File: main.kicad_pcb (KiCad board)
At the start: 2 copper layers, 31.3 x 52.8 mm, 21 parts

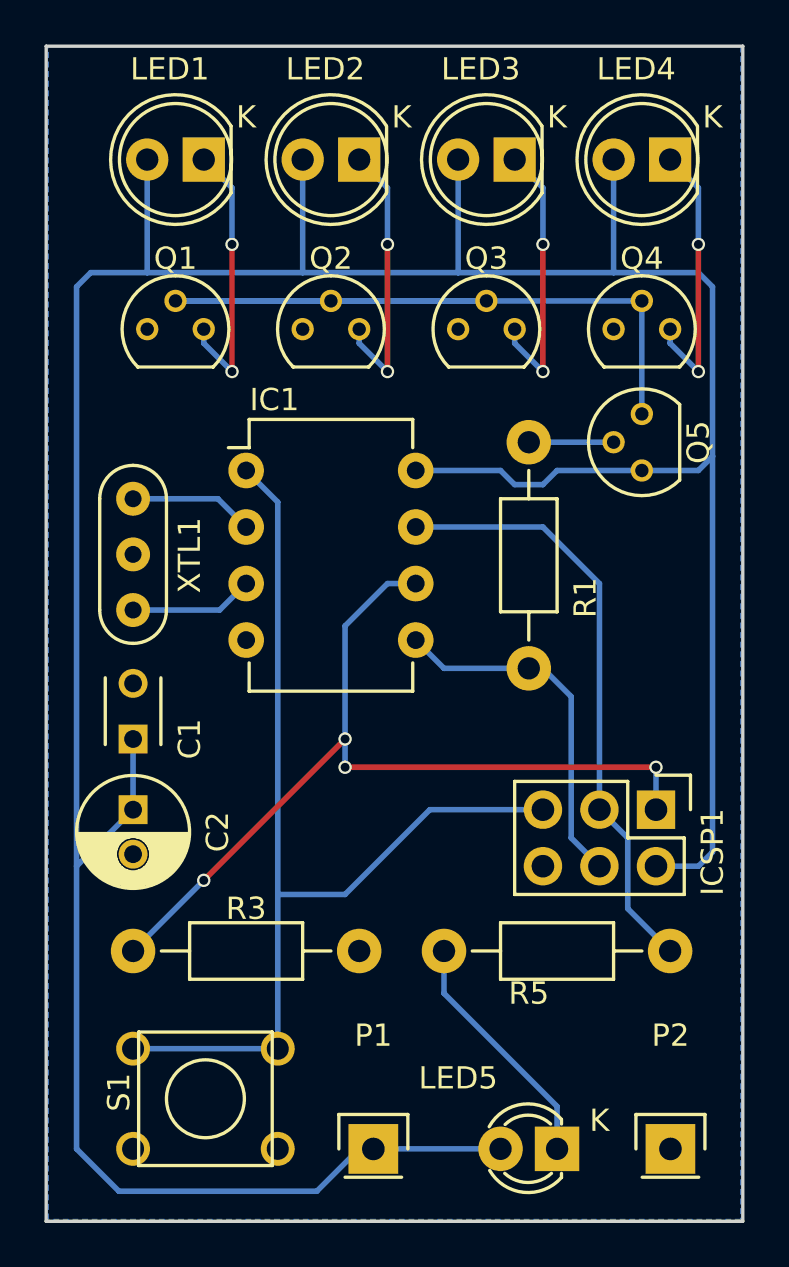
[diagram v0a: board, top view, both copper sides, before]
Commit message: new vias
bigger and better for cnc
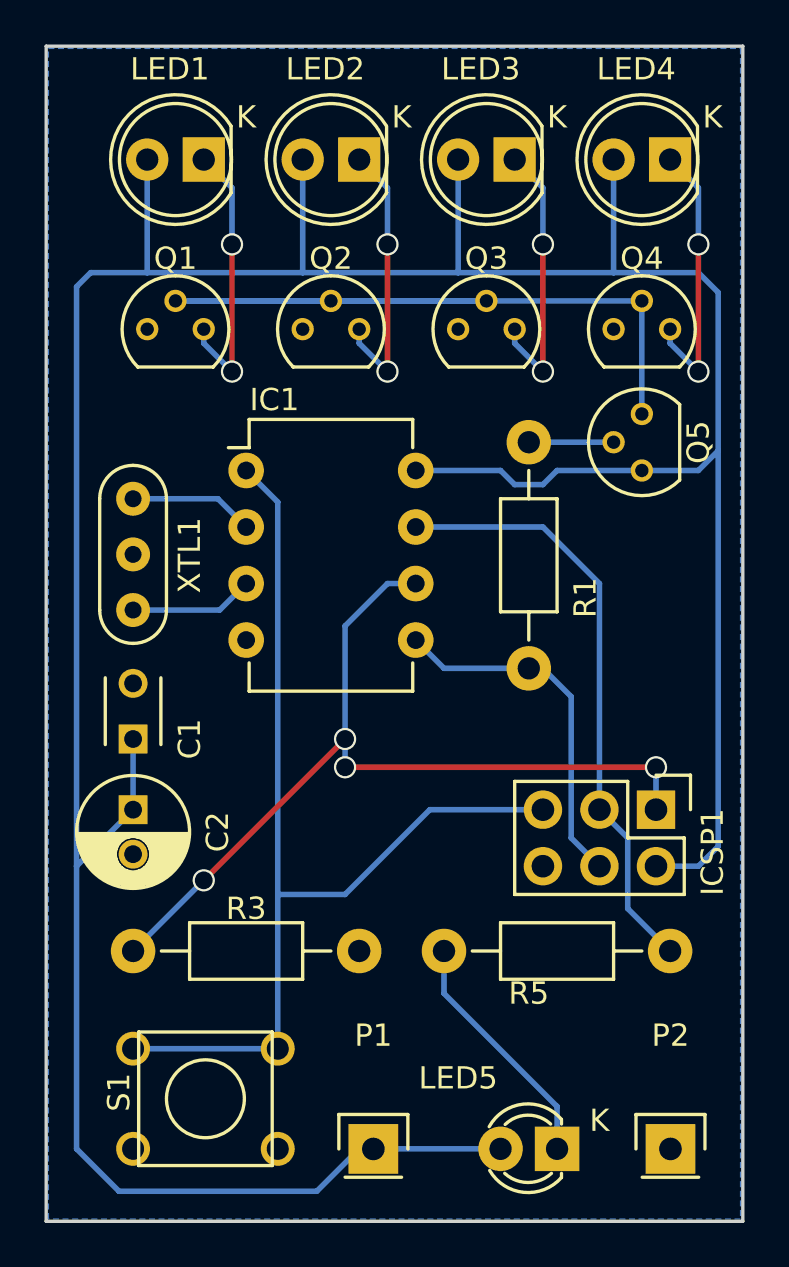
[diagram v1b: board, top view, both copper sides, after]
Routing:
- net VCC: track 158.5 -> 159.1 mm
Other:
- net class Default: via_dia 0.8 -> 1; via_drill 0.7 -> 0.8
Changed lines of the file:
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@@
     (links 43)
     (no_connects 0)
-    (area 148.95 69.106 181.875 122.62)
+    (area 150.324999 69.124999 181.775001 122.075001)
     (thickness 1.6)
     (drawings 5)
@@
     (segment_width 0.2)
     (edge_width 0.15)
-    (via_size 0.8)
-    (via_drill 0.7)
+    (via_size 1)
+    (via_drill 0.8)
     (via_min_size 0.4)
     (via_min_drill 0.3)
@@
     (clearance 0.2)
     (trace_width 0.25)
-    (via_dia 0.8)
-    (via_drill 0.7)
+    (via_dia 1)
+    (via_drill 0.8)
     (uvia_dia 0.3)
     (uvia_drill 0.1)
@@
   )
   (gr_text ".pls GS" (at 177.7 96.2 90) (layer Dwgs.User)
-    (effects (font (size 1.5 1.5) (thickness 0.3)))
+    (effects (font (size 1.5 1.5) (thickness 0.3)) (justify mirror))
   )
   (gr_line (start 150.4 69.2) (end 181.7 69.2) (angle 90) (layer Edge.Cuts) (width 0.15))
@@
   (gr_line (start 150.4 122) (end 181.7 122) (angle 90) (layer Edge.Cuts) (width 0.15))
   (segment (start 152.4 79.375) (end 151.765 80.01) (width 0.25) (layer B.Cu) (net 1))
-  (segment (start 180.34 87.63) (end 180.34 105.41) (width 0.25) (layer B.Cu) (net 1))
+  (segment (start 180.594 87.376) (end 180.594 105.156) (width 0.25) (layer B.Cu) (net 1))
   (segment (start 179.705 106.045) (end 177.8 106.045) (width 0.25) (layer B.Cu) (net 1))
-  (segment (start 180.34 105.41) (end 179.705 106.045) (width 0.25) (layer B.Cu) (net 1))
+  (segment (start 180.594 105.156) (end 179.705 106.045) (width 0.25) (layer B.Cu) (net 1))
   (segment (start 170.815 118.745) (end 170.815 119.38) (width 0.25) (layer B.Cu) (net 1))
   (segment (start 177.165 88.265) (end 173.355 88.265) (width 0.25) (layer B.Cu) (net 1))
@@
   (segment (start 175.895 79.375) (end 179.705 79.375) (width 0.25) (layer B.Cu) (net 1))
   (segment (start 179.705 88.265) (end 177.165 88.265) (width 0.25) (layer B.Cu) (net 1))
-  (segment (start 180.34 87.63) (end 179.705 88.265) (width 0.25) (layer B.Cu) (net 1))
-  (segment (start 180.34 80.01) (end 180.34 87.63) (width 0.25) (layer B.Cu) (net 1))
-  (segment (start 179.705 79.375) (end 180.34 80.01) (width 0.25) (layer B.Cu) (net 1))
+  (segment (start 180.594 87.376) (end 179.705 88.265) (width 0.25) (layer B.Cu) (net 1))
+  (segment (start 180.594 80.264) (end 180.594 87.376) (width 0.25) (layer B.Cu) (net 1))
+  (segment (start 179.705 79.375) (end 180.594 80.264) (width 0.25) (layer B.Cu) (net 1))
   (segment (start 154.94 79.375) (end 154.94 74.295) (width 0.25) (layer B.Cu) (net 1))
   (segment (start 161.925 79.375) (end 161.925 74.295) (width 0.25) (layer B.Cu) (net 1))
@@
   (segment (start 163.83 100.33) (end 163.83 101.6) (width 0.25) (layer B.Cu) (net 7))
   (segment (start 177.8 101.6) (end 177.8 103.505) (width 0.25) (layer B.Cu) (net 7))
-  (via (at 177.8 101.6) (size 0.6) (drill 0.4) (layers F.Cu B.Cu) (net 7))
+  (via (at 177.8 101.6) (size 1) (drill 0.8) (layers F.Cu B.Cu) (net 7))
   (segment (start 163.83 101.6) (end 177.8 101.6) (width 0.25) (layer F.Cu) (net 7))
-  (via (at 163.83 101.6) (size 0.6) (drill 0.4) (layers F.Cu B.Cu) (net 7))
+  (via (at 163.83 101.6) (size 1) (drill 0.8) (layers F.Cu B.Cu) (net 7))
   (segment (start 154.305 109.855) (end 157.48 106.68) (width 0.25) (layer B.Cu) (net 7))
   (segment (start 165.735 93.345) (end 167.005 93.345) (width 0.25) (layer B.Cu) (net 7))
   (segment (start 163.83 95.25) (end 165.735 93.345) (width 0.25) (layer B.Cu) (net 7))
   (segment (start 163.83 100.33) (end 163.83 95.25) (width 0.25) (layer B.Cu) (net 7))
-  (via (at 163.83 100.33) (size 0.6) (drill 0.4) (layers F.Cu B.Cu) (net 7))
+  (via (at 163.83 100.33) (size 1) (drill 0.8) (layers F.Cu B.Cu) (net 7))
   (segment (start 157.48 106.68) (end 163.83 100.33) (width 0.25) (layer F.Cu) (net 7))
-  (via (at 157.48 106.68) (size 0.6) (drill 0.4) (layers F.Cu B.Cu) (net 7))
+  (via (at 157.48 106.68) (size 1) (drill 0.8) (layers F.Cu B.Cu) (net 7))
   (segment (start 178.435 109.855) (end 176.53 107.95) (width 0.25) (layer B.Cu) (net 8))
   (segment (start 176.53 104.775) (end 175.26 103.505) (width 0.25) (layer B.Cu) (net 8))
@@
   (segment (start 158.75 75.565) (end 157.48 74.295) (width 0.25) (layer B.Cu) (net 9))
   (segment (start 158.75 78.105) (end 158.75 75.565) (width 0.25) (layer B.Cu) (net 9))
-  (via (at 158.75 78.105) (size 0.6) (drill 0.4) (layers F.Cu B.Cu) (net 9))
+  (via (at 158.75 78.105) (size 1) (drill 0.8) (layers F.Cu B.Cu) (net 9))
   (segment (start 158.75 83.82) (end 158.75 78.105) (width 0.25) (layer F.Cu) (net 9))
-  (via (at 158.75 83.82) (size 0.6) (drill 0.4) (layers F.Cu B.Cu) (net 9))
+  (via (at 158.75 83.82) (size 1) (drill 0.8) (layers F.Cu B.Cu) (net 9))
   (segment (start 157.48 82.55) (end 158.75 83.82) (width 0.25) (layer B.Cu) (net 9))
   (segment (start 164.465 81.915) (end 164.465 82.55) (width 0.25) (layer B.Cu) (net 10))
   (segment (start 165.735 75.565) (end 164.465 74.295) (width 0.25) (layer B.Cu) (net 10))
   (segment (start 165.735 78.105) (end 165.735 75.565) (width 0.25) (layer B.Cu) (net 10))
-  (via (at 165.735 78.105) (size 0.6) (drill 0.4) (layers F.Cu B.Cu) (net 10))
+  (via (at 165.735 78.105) (size 1) (drill 0.8) (layers F.Cu B.Cu) (net 10))
   (segment (start 165.735 83.82) (end 165.735 78.105) (width 0.25) (layer F.Cu) (net 10))
-  (via (at 165.735 83.82) (size 0.6) (drill 0.4) (layers F.Cu B.Cu) (net 10))
+  (via (at 165.735 83.82) (size 1) (drill 0.8) (layers F.Cu B.Cu) (net 10))
   (segment (start 164.465 82.55) (end 165.735 83.82) (width 0.25) (layer B.Cu) (net 10))
   (segment (start 171.45 81.915) (end 171.45 82.55) (width 0.25) (layer B.Cu) (net 11))
   (segment (start 172.72 75.565) (end 171.45 74.295) (width 0.25) (layer B.Cu) (net 11))
   (segment (start 172.72 78.105) (end 172.72 75.565) (width 0.25) (layer B.Cu) (net 11))
-  (via (at 172.72 78.105) (size 0.6) (drill 0.4) (layers F.Cu B.Cu) (net 11))
+  (via (at 172.72 78.105) (size 1) (drill 0.8) (layers F.Cu B.Cu) (net 11))
   (segment (start 172.72 83.82) (end 172.72 78.105) (width 0.25) (layer F.Cu) (net 11))
-  (via (at 172.72 83.82) (size 0.6) (drill 0.4) (layers F.Cu B.Cu) (net 11))
+  (via (at 172.72 83.82) (size 1) (drill 0.8) (layers F.Cu B.Cu) (net 11))
   (segment (start 171.45 82.55) (end 172.72 83.82) (width 0.25) (layer B.Cu) (net 11))
   (segment (start 178.435 81.915) (end 178.435 82.55) (width 0.25) (layer B.Cu) (net 12))
   (segment (start 179.705 75.565) (end 178.435 74.295) (width 0.25) (layer B.Cu) (net 12))
   (segment (start 179.705 78.105) (end 179.705 75.565) (width 0.25) (layer B.Cu) (net 12))
-  (via (at 179.705 78.105) (size 0.6) (drill 0.4) (layers F.Cu B.Cu) (net 12))
+  (via (at 179.705 78.105) (size 1) (drill 0.8) (layers F.Cu B.Cu) (net 12))
   (segment (start 179.705 83.82) (end 179.705 78.105) (width 0.25) (layer F.Cu) (net 12))
-  (via (at 179.705 83.82) (size 0.6) (drill 0.4) (layers F.Cu B.Cu) (net 12))
+  (via (at 179.705 83.82) (size 1) (drill 0.8) (layers F.Cu B.Cu) (net 12))
   (segment (start 178.435 82.55) (end 179.705 83.82) (width 0.25) (layer B.Cu) (net 12))
   (segment (start 173.355 118.745) (end 173.355 116.84) (width 0.25) (layer B.Cu) (net 13))
@@
   (segment (start 175.895 86.995) (end 172.085 86.995) (width 0.25) (layer B.Cu) (net 15))
   (zone (net 2) (net_name GND) (layer B.Cu) (hatch edge 0.508)
-    (connect_pads (clearance 0.508))
+    (connect_pads yes (clearance 0.508))
     (min_thickness 0.254)
     (fill yes (arc_segments 16) (thermal_gap 0.508) (thermal_bridge_width 0.508))
     (polygon
       (pts
-        (xy 181.61 121.92) (xy 150.495 121.92) (xy 150.495 69.215) (xy 181.61 69.215) (xy 181.61 121.92)
+        (xy 181.6 121.9) (xy 150.5 121.9) (xy 150.5 69.3) (xy 181.6 69.3) (xy 181.6 121.9)
       )
     )

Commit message: logo
pacman logo added
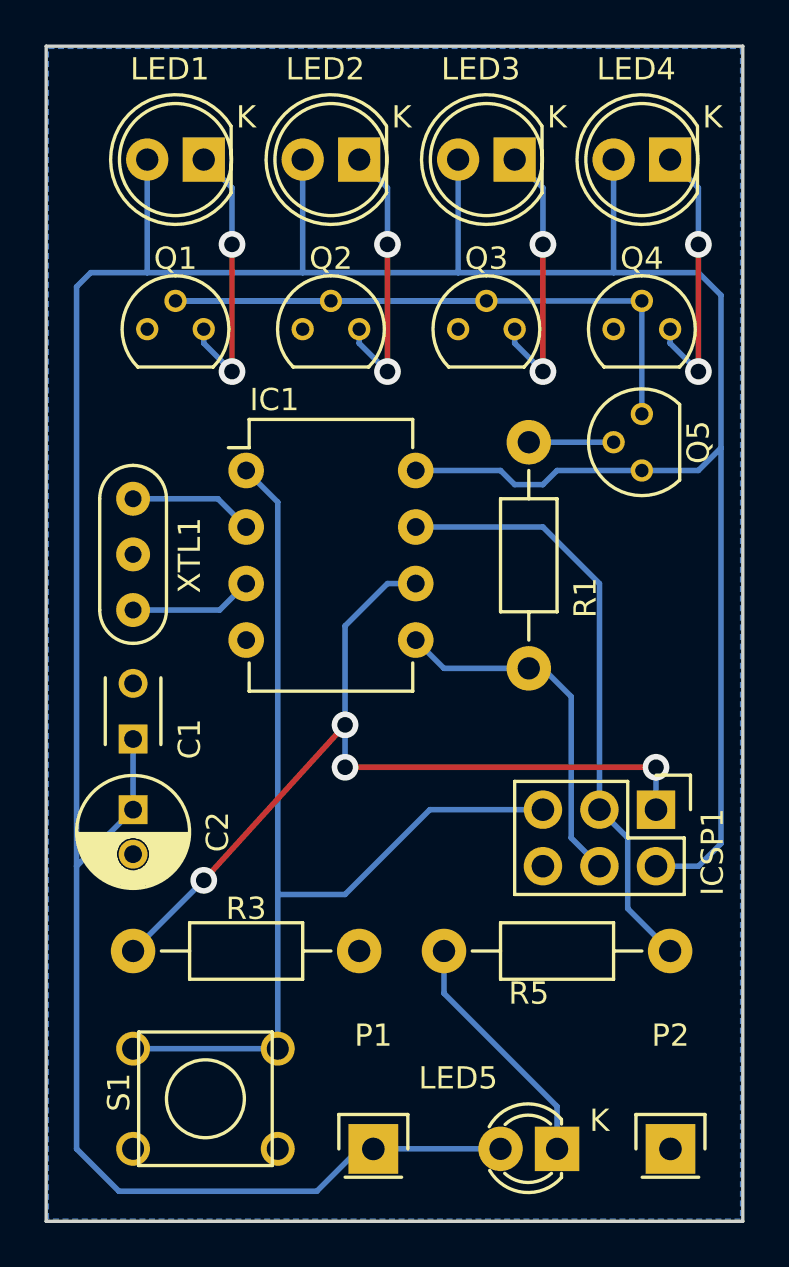
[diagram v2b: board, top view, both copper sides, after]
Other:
- net class Default: via_dia 1 -> 1.2; via_drill 0.8 -> 0.7
- board text added: "GS"
- board text removed: ".pls GS"
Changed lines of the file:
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@@
     (area 150.324999 69.124999 181.775001 122.075001)
     (thickness 1.6)
-    (drawings 5)
+    (drawings 11)
     (tracks 102)
     (zones 0)
@@
     (segment_width 0.2)
     (edge_width 0.15)
-    (via_size 1)
-    (via_drill 0.8)
+    (via_size 1.2)
+    (via_drill 0.7)
     (via_min_size 0.4)
     (via_min_drill 0.3)
@@
     (clearance 0.2)
     (trace_width 0.25)
-    (via_dia 1)
-    (via_drill 0.8)
+    (via_dia 1.2)
+    (via_drill 0.7)
     (uvia_dia 0.3)
     (uvia_drill 0.1)
@@
     )
   )
-  (gr_text ".pls GS" (at 177.7 96.2 90) (layer Dwgs.User)
+  (gr_arc (start 178.054 96.774) (end 178.816 96.012) (angle 90) (layer Dwgs.User) (width 0.2))
+  (gr_arc (start 178.054 96.774) (end 178.816 97.536) (angle 90) (layer Dwgs.User) (width 0.2))
+  (gr_arc (start 178.054 96.774) (end 177.292 97.536) (angle 90) (layer Dwgs.User) (width 0.2))
+  (gr_line (start 178.054 96.774) (end 177.292 96.012) (angle 90) (layer Dwgs.User) (width 0.2))
+  (gr_line (start 178.816 96.012) (end 178.054 96.774) (angle 90) (layer Dwgs.User) (width 0.2))
+  (gr_line (start 178.054 96.774) (end 178.816 96.012) (angle 90) (layer Dwgs.User) (width 0.2))
+  (gr_text GS (at 177.927 94.361 270) (layer Dwgs.User)
     (effects (font (size 1.5 1.5) (thickness 0.3)) (justify mirror))
   )
@@
   (gr_line (start 150.4 122) (end 181.7 122) (angle 90) (layer Edge.Cuts) (width 0.15))
   (segment (start 152.4 79.375) (end 151.765 80.01) (width 0.25) (layer B.Cu) (net 1))
-  (segment (start 180.594 87.376) (end 180.594 105.156) (width 0.25) (layer B.Cu) (net 1))
+  (segment (start 180.721 87.249) (end 180.721 105.029) (width 0.25) (layer B.Cu) (net 1))
   (segment (start 179.705 106.045) (end 177.8 106.045) (width 0.25) (layer B.Cu) (net 1))
-  (segment (start 180.594 105.156) (end 179.705 106.045) (width 0.25) (layer B.Cu) (net 1))
+  (segment (start 180.721 105.029) (end 179.705 106.045) (width 0.25) (layer B.Cu) (net 1))
   (segment (start 170.815 118.745) (end 170.815 119.38) (width 0.25) (layer B.Cu) (net 1))
   (segment (start 177.165 88.265) (end 173.355 88.265) (width 0.25) (layer B.Cu) (net 1))
@@
   (segment (start 175.895 79.375) (end 179.705 79.375) (width 0.25) (layer B.Cu) (net 1))
   (segment (start 179.705 88.265) (end 177.165 88.265) (width 0.25) (layer B.Cu) (net 1))
-  (segment (start 180.594 87.376) (end 179.705 88.265) (width 0.25) (layer B.Cu) (net 1))
-  (segment (start 180.594 80.264) (end 180.594 87.376) (width 0.25) (layer B.Cu) (net 1))
-  (segment (start 179.705 79.375) (end 180.594 80.264) (width 0.25) (layer B.Cu) (net 1))
+  (segment (start 180.721 87.249) (end 179.705 88.265) (width 0.25) (layer B.Cu) (net 1))
+  (segment (start 180.721 80.391) (end 180.721 87.249) (width 0.25) (layer B.Cu) (net 1))
+  (segment (start 179.705 79.375) (end 180.721 80.391) (width 0.25) (layer B.Cu) (net 1))
   (segment (start 154.94 79.375) (end 154.94 74.295) (width 0.25) (layer B.Cu) (net 1))
   (segment (start 161.925 79.375) (end 161.925 74.295) (width 0.25) (layer B.Cu) (net 1))
@@
   (segment (start 172.72 97.155) (end 168.275 97.155) (width 0.25) (layer B.Cu) (net 6))
   (segment (start 168.275 97.155) (end 167.005 95.885) (width 0.25) (layer B.Cu) (net 6))
-  (segment (start 163.83 100.33) (end 163.83 101.6) (width 0.25) (layer B.Cu) (net 7))
+  (segment (start 163.83 99.695) (end 163.83 101.6) (width 0.25) (layer B.Cu) (net 7))
   (segment (start 177.8 101.6) (end 177.8 103.505) (width 0.25) (layer B.Cu) (net 7))
-  (via (at 177.8 101.6) (size 1) (drill 0.8) (layers F.Cu B.Cu) (net 7))
+  (via (at 177.8 101.6) (size 1.2) (drill 0.7) (layers F.Cu B.Cu) (net 7))
   (segment (start 163.83 101.6) (end 177.8 101.6) (width 0.25) (layer F.Cu) (net 7))
-  (via (at 163.83 101.6) (size 1) (drill 0.8) (layers F.Cu B.Cu) (net 7))
+  (via (at 163.83 101.6) (size 1.2) (drill 0.7) (layers F.Cu B.Cu) (net 7))
   (segment (start 154.305 109.855) (end 157.48 106.68) (width 0.25) (layer B.Cu) (net 7))
   (segment (start 165.735 93.345) (end 167.005 93.345) (width 0.25) (layer B.Cu) (net 7))
   (segment (start 163.83 95.25) (end 165.735 93.345) (width 0.25) (layer B.Cu) (net 7))
-  (segment (start 163.83 100.33) (end 163.83 95.25) (width 0.25) (layer B.Cu) (net 7))
-  (via (at 163.83 100.33) (size 1) (drill 0.8) (layers F.Cu B.Cu) (net 7))
-  (segment (start 157.48 106.68) (end 163.83 100.33) (width 0.25) (layer F.Cu) (net 7))
-  (via (at 157.48 106.68) (size 1) (drill 0.8) (layers F.Cu B.Cu) (net 7))
+  (segment (start 163.83 99.695) (end 163.83 95.25) (width 0.25) (layer B.Cu) (net 7))
+  (via (at 163.83 99.695) (size 1.2) (drill 0.7) (layers F.Cu B.Cu) (net 7))
+  (segment (start 157.48 106.68) (end 163.83 99.695) (width 0.25) (layer F.Cu) (net 7))
+  (via (at 157.48 106.68) (size 1.2) (drill 0.7) (layers F.Cu B.Cu) (net 7))
   (segment (start 178.435 109.855) (end 176.53 107.95) (width 0.25) (layer B.Cu) (net 8))
   (segment (start 176.53 104.775) (end 175.26 103.505) (width 0.25) (layer B.Cu) (net 8))
@@
   (segment (start 158.75 75.565) (end 157.48 74.295) (width 0.25) (layer B.Cu) (net 9))
   (segment (start 158.75 78.105) (end 158.75 75.565) (width 0.25) (layer B.Cu) (net 9))
-  (via (at 158.75 78.105) (size 1) (drill 0.8) (layers F.Cu B.Cu) (net 9))
+  (via (at 158.75 78.105) (size 1.2) (drill 0.7) (layers F.Cu B.Cu) (net 9))
   (segment (start 158.75 83.82) (end 158.75 78.105) (width 0.25) (layer F.Cu) (net 9))
-  (via (at 158.75 83.82) (size 1) (drill 0.8) (layers F.Cu B.Cu) (net 9))
+  (via (at 158.75 83.82) (size 1.2) (drill 0.7) (layers F.Cu B.Cu) (net 9))
   (segment (start 157.48 82.55) (end 158.75 83.82) (width 0.25) (layer B.Cu) (net 9))
   (segment (start 164.465 81.915) (end 164.465 82.55) (width 0.25) (layer B.Cu) (net 10))
   (segment (start 165.735 75.565) (end 164.465 74.295) (width 0.25) (layer B.Cu) (net 10))
   (segment (start 165.735 78.105) (end 165.735 75.565) (width 0.25) (layer B.Cu) (net 10))
-  (via (at 165.735 78.105) (size 1) (drill 0.8) (layers F.Cu B.Cu) (net 10))
+  (via (at 165.735 78.105) (size 1.2) (drill 0.7) (layers F.Cu B.Cu) (net 10))
   (segment (start 165.735 83.82) (end 165.735 78.105) (width 0.25) (layer F.Cu) (net 10))
-  (via (at 165.735 83.82) (size 1) (drill 0.8) (layers F.Cu B.Cu) (net 10))
+  (via (at 165.735 83.82) (size 1.2) (drill 0.7) (layers F.Cu B.Cu) (net 10))
   (segment (start 164.465 82.55) (end 165.735 83.82) (width 0.25) (layer B.Cu) (net 10))
   (segment (start 171.45 81.915) (end 171.45 82.55) (width 0.25) (layer B.Cu) (net 11))
   (segment (start 172.72 75.565) (end 171.45 74.295) (width 0.25) (layer B.Cu) (net 11))
   (segment (start 172.72 78.105) (end 172.72 75.565) (width 0.25) (layer B.Cu) (net 11))
-  (via (at 172.72 78.105) (size 1) (drill 0.8) (layers F.Cu B.Cu) (net 11))
+  (via (at 172.72 78.105) (size 1.2) (drill 0.7) (layers F.Cu B.Cu) (net 11))
   (segment (start 172.72 83.82) (end 172.72 78.105) (width 0.25) (layer F.Cu) (net 11))
-  (via (at 172.72 83.82) (size 1) (drill 0.8) (layers F.Cu B.Cu) (net 11))
+  (via (at 172.72 83.82) (size 1.2) (drill 0.7) (layers F.Cu B.Cu) (net 11))
   (segment (start 171.45 82.55) (end 172.72 83.82) (width 0.25) (layer B.Cu) (net 11))
   (segment (start 178.435 81.915) (end 178.435 82.55) (width 0.25) (layer B.Cu) (net 12))
   (segment (start 179.705 75.565) (end 178.435 74.295) (width 0.25) (layer B.Cu) (net 12))
   (segment (start 179.705 78.105) (end 179.705 75.565) (width 0.25) (layer B.Cu) (net 12))
-  (via (at 179.705 78.105) (size 1) (drill 0.8) (layers F.Cu B.Cu) (net 12))
+  (via (at 179.705 78.105) (size 1.2) (drill 0.7) (layers F.Cu B.Cu) (net 12))
   (segment (start 179.705 83.82) (end 179.705 78.105) (width 0.25) (layer F.Cu) (net 12))
-  (via (at 179.705 83.82) (size 1) (drill 0.8) (layers F.Cu B.Cu) (net 12))
+  (via (at 179.705 83.82) (size 1.2) (drill 0.7) (layers F.Cu B.Cu) (net 12))
   (segment (start 178.435 82.55) (end 179.705 83.82) (width 0.25) (layer B.Cu) (net 12))
   (segment (start 173.355 118.745) (end 173.355 116.84) (width 0.25) (layer B.Cu) (net 13))
